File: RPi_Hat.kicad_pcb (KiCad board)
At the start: 2 copper layers, 65 x 56.5 mm, 5 parts, among them J2 RPi_GPIO

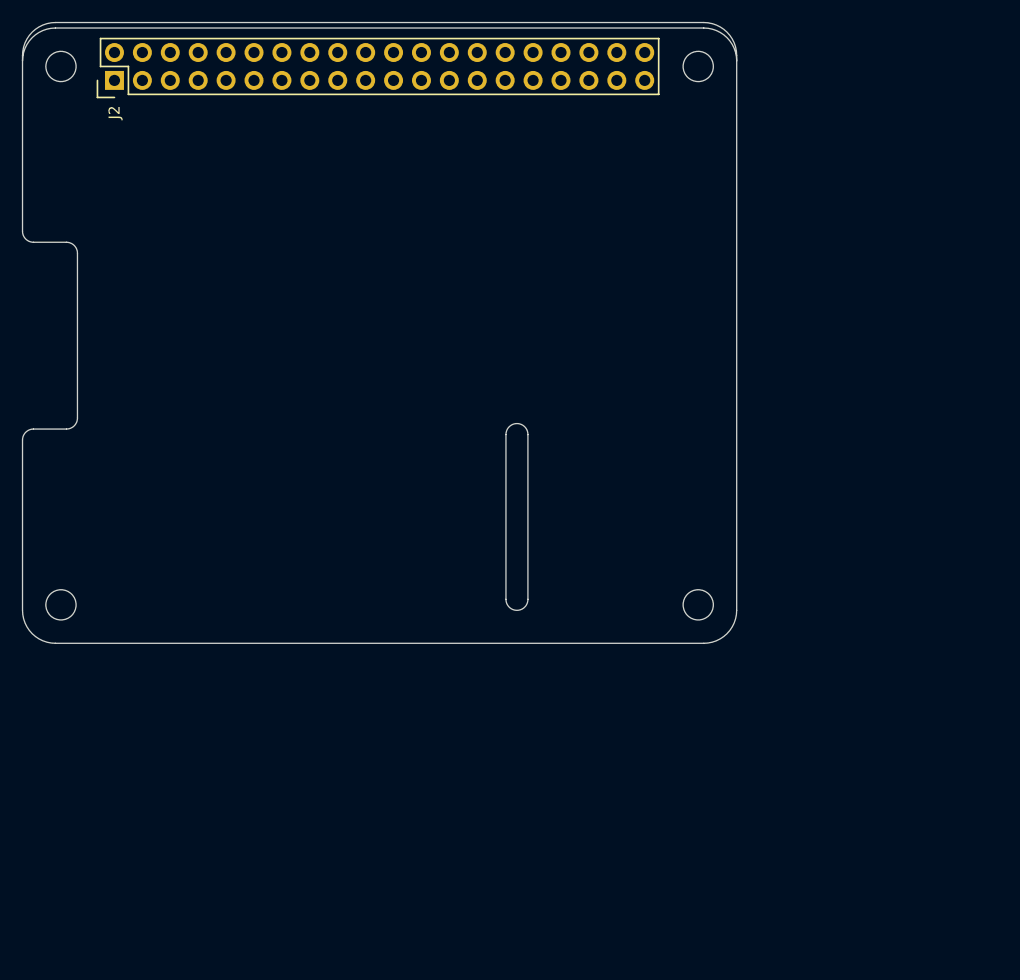
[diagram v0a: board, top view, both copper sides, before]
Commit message: Added components to schematic
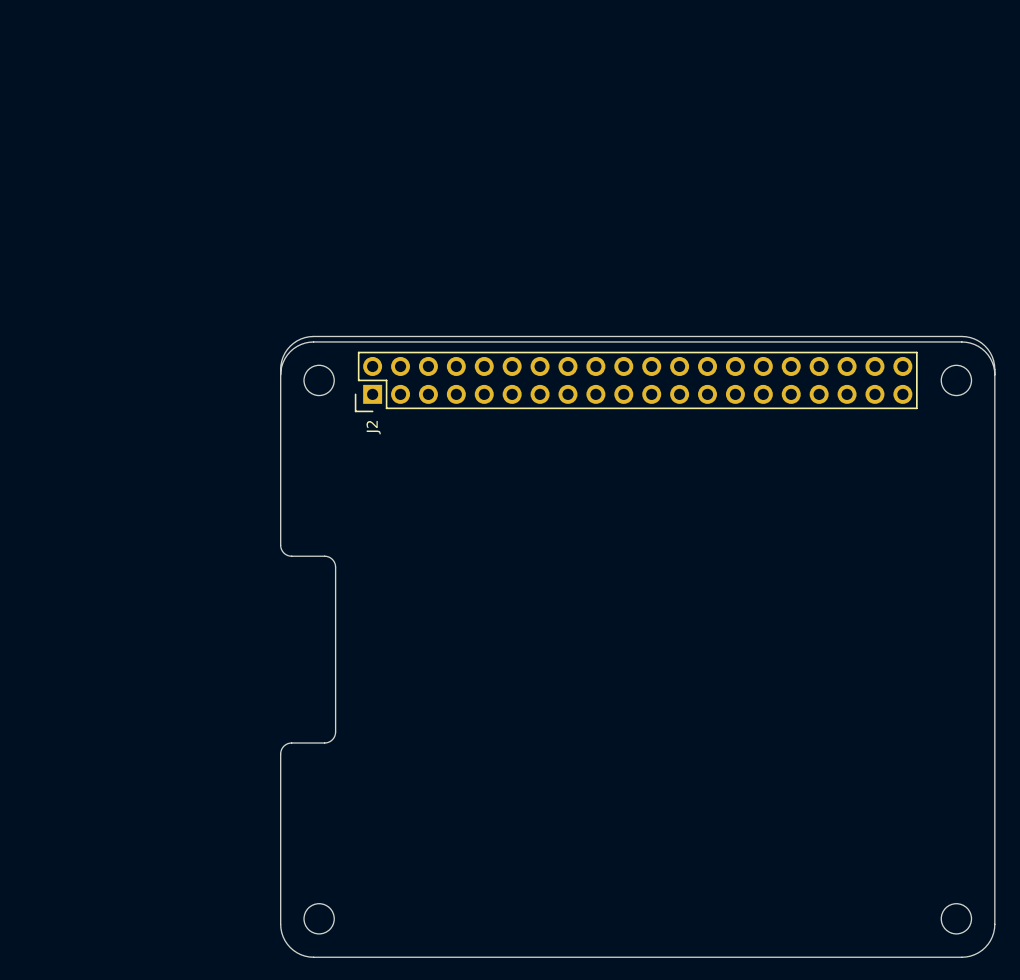
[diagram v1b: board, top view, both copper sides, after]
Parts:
- moved ? 37.0 mm to (85.0, 32.6)
- moved ? 37.0 mm to (85.0, 81.6)
- moved ? 37.0 mm to (27.0, 81.6)
- moved ? 37.0 mm to (27.0, 32.6)
- moved J2 37.0 mm to (56.0, 32.6)
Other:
- outline, holes or cut-outs redrawn
- board text removed: "Camera Flex Slot (Optional)"

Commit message: Layed out PCB
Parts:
- added BZ1: Buzzer, Buzzers_Beepers:Buzzer_12x9.5RM7.6, F.Cu at (61.1, 39.0)
- added C1: 100nF, Capacitors_THT:C_Disc_D4.7mm_W2.5mm_P5.00mm, F.Cu at (27.9, 40.6)
- added D1: LED, LEDs:LED_D5.0mm, F.Cu at (76.8, 82.5)
- added IC1: 0.96_I2C_OLED, IIC_OLED:0.91_I2C_OLED, F.Cu at (48.3, 58.4)
- added IC2: 7406, Housings_DIP:DIP-14_W7.62mm_Socket, F.Cu at (31.8, 47.0)
- added IC3: I2C LC, IIC_4CH_Level_Converter:4CH_I2C_Level_Converter, F.Cu at (41.9, 55.9)
- added IEC 1: C64_IEC, C64_IEC:C64_IEC, F.Cu at (76.2, 46.4)
- added IEC 2: C64_IEC, C64_IEC:C64_IEC, F.Cu at (76.2, 67.9)
- added R1: 100, Resistors_THT:R_Axial_DIN0207_L6.3mm_D2.5mm_P10.16mm_Horizontal, F.Cu at (68.6, 52.1)
- added R2: 1K, Resistors_THT:R_Axial_DIN0207_L6.3mm_D2.5mm_P10.16mm_Horizontal, F.Cu at (64.8, 62.2)
- added R3: 1K, Resistors_THT:R_Axial_DIN0207_L6.3mm_D2.5mm_P10.16mm_Horizontal, F.Cu at (61.0, 62.2)
- added SW1: Select, Buttons_Switches_THT:SW_PUSH_6mm_h5mm, F.Cu at (36.8, 76.8)
- added SW2: Up, Buttons_Switches_THT:SW_PUSH_6mm_h5mm, F.Cu at (45.1, 76.8)
- added SW3: Down, Buttons_Switches_THT:SW_PUSH_6mm_h5mm, F.Cu at (53.3, 76.8)
- added SW4: Exit, Buttons_Switches_THT:SW_PUSH_6mm_h5mm, F.Cu at (61.6, 76.8)
- added SW5: Add Disk, Buttons_Switches_THT:SW_PUSH_6mm_h5mm, F.Cu at (69.8, 76.8)
- renumbered J2 to J1
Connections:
- J1 pad 1: (no net) -> +3V3
- J1 pad 11: (no net) -> RPI_CLK_OUT
- J1 pad 12: (no net) -> RPI_DATA_OUT
- J1 pad 13: (no net) -> IN_SW1
- J1 pad 14: (no net) -> GND
- J1 pad 15: (no net) -> IN_SW2
- J1 pad 16: (no net) -> IN_SW3
- J1 pad 18: (no net) -> RPI_ATN
- J1 pad 2: (no net) -> +5V
- J1 pad 20: (no net) -> GND
- J1 pad 22: (no net) -> RPI_DATA_IN
- J1 pad 25: (no net) -> GND
- J1 pad 29: (no net) -> IN_SW5
- J1 pad 3: (no net) -> I2C_SDA
- J1 pad 30: (no net) -> GND
- J1 pad 33: (no net) -> RPI_SND
- J1 pad 34: (no net) -> GND
- J1 pad 36: (no net) -> RPI_LED
- J1 pad 37: (no net) -> RPI_CLK_IN
- J1 pad 38: (no net) -> RPI_RST
- J1 pad 39: (no net) -> GND
- J1 pad 5: (no net) -> I2C_SCL
- J1 pad 6: (no net) -> GND
- J1 pad 7: (no net) -> IN_SW4
- J1 pad 9: (no net) -> GND
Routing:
- net C64_DATA: track 0.00 -> 78.7 mm, vias 0 -> 1
- net +5V: track 0.00 -> 76.6 mm
- net IN_SW1: track 0.00 -> 73.7 mm, vias 0 -> 2
- net RPI_CLK_IN: track 0.00 -> 73.4 mm, vias 0 -> 2
- net C64_CLK: track 0.00 -> 73.2 mm, vias 0 -> 3
- net IN_SW5: track 0.00 -> 68.6 mm, vias 0 -> 2
- net IN_SW2: track 0.00 -> 65.4 mm, vias 0 -> 2
- net C64_ATN: track 0.00 -> 61.3 mm, vias 0 -> 1
- net IN_SW3: track 0.00 -> 60.9 mm, vias 0 -> 2
- net IN_SW4: track 0.00 -> 59.7 mm, vias 0 -> 2
- net RPI_LED: track 0.00 -> 55.5 mm
- net RPI_RST: track 0.00 -> 54.5 mm, vias 0 -> 2
- net RPI_ATN: track 0.00 -> 50.3 mm, vias 0 -> 2
- net C64_RST: track 0.00 -> 49.4 mm
- net RPI_DATA_IN: track 0.00 -> 35.6 mm, vias 0 -> 2
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- added copper zone on B.Cu, net GND
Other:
- outline, holes or cut-outs redrawn
- board text added: "ADD"
- board text added: "BACK"
- board text added: "BROWSE"
- board text added: "DOWN"
- board text added: "EMULATION"
- board text added: "EXIT"
- board text added: "MODE"
- board text added: "NEXT"
- board text added: "Pi1541"
- board text added: "SELECT"
- board text added: "UP"
- board text added: "https://cbm-pi1541.firebaseapp.com"
- board text added: "https://hvetebolle.blogspot.com"

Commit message: Added silkscreen info.
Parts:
- IEC #1: renamed from IEC 1
- IEC #2: renamed from IEC 2
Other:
- board text added: "PCB Rev. A"
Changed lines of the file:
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@@
     (area 23.444999 28.524999 88.545001 85.125001)
     (thickness 1.6)
-    (drawings 41)
+    (drawings 42)
     (tracks 347)
     (zones 0)
@@
   (module C64_IEC:C64_IEC (layer F.Cu)
     (at 76.2 46.355 90)
-    (fp_text reference "IEC 1" (at 0.127 4.826 90) (layer B.SilkS)
+    (fp_text reference "IEC #1" (at 0.127 4.826 90) (layer B.SilkS)
       (effects (font (size 2 2) (thickness 0.15)) (justify mirror))
     )
@@
   (module C64_IEC:C64_IEC (layer F.Cu)
     (at 76.2 67.945 90)
-    (fp_text reference "IEC 2" (at 0.127 4.826 90) (layer B.SilkS)
+    (fp_text reference "IEC #2" (at 0.127 4.826 90) (layer B.SilkS)
       (effects (font (size 2 2) (thickness 0.15)) (justify mirror))
     )
@@
       (net 6 I2C_SDA))
   )
-  (gr_text https://hvetebolle.blogspot.com (at 69.596 73.66) (layer B.SilkS)
+  (gr_text "PCB Rev. A" (at 29.718 57.15 270) (layer F.SilkS)
+    (effects (font (size 1.5 1.5) (thickness 0.3)))
+  )
+  (gr_text https://hvetebolle.blogspot.com (at 73.66 81.28) (layer B.SilkS)
     (effects (font (size 1.5 1.5) (thickness 0.3)) (justify left mirror))
   )
-  (gr_text https://cbm-pi1541.firebaseapp.com (at 69.596 71.12) (layer B.SilkS)
+  (gr_text https://cbm-pi1541.firebaseapp.com (at 73.66 79.248) (layer B.SilkS)
     (effects (font (size 1.5 1.5) (thickness 0.3)) (justify left mirror))
   )
-  (gr_text Pi1541 (at 61.722 66.802) (layer B.SilkS)
-    (effects (font (size 4 4) (thickness 0.4) italic) (justify left mirror))
+  (gr_text Pi1541 (at 39.37 43.434) (layer B.SilkS)
+    (effects (font (size 4 4) (thickness 0.4) italic) (justify mirror))
   )
   (gr_text MODE (at 27.178 69.088) (layer F.SilkS)
